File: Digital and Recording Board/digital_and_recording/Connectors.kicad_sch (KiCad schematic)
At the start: 14 parts, among them J1 Headphones, J2 Screen, J3 USB_Breakout, J4 Joystick, J5 Conn_02x20_Odd_Even, U3 Bypass 2, U4 Bypass 1, U5 Output Select

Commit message: updated schematic to use +/-5 DCDC
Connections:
- net +5V: now also C2.2, C4.1, C7.2, U3.4 (V+), U4.4 (V+), U5.4 (V+)
- net Guitar_In: now also J5.25 (Pin_25), J5.26 (Pin_26), J5.27 (Pin_27), J5.28 (Pin_28); no longer J5.37 (Pin_37), J5.38 (Pin_38), J5.39 (Pin_39), J5.40 (Pin_40)
- removed net +6V: C2.2, C4.1, C7.2, J5.13 (Pin_13), J5.14 (Pin_14), J5.15 (Pin_15), J5.16 (Pin_16), U3.4 (V+), U4.4 (V+), U5.4 (V+)
- net -6V renamed -5V
- net -5V: no longer J5.19 (Pin_19), J5.20 (Pin_20), J5.21 (Pin_21), J5.22 (Pin_22)
- no-connect marks 16 -> 24

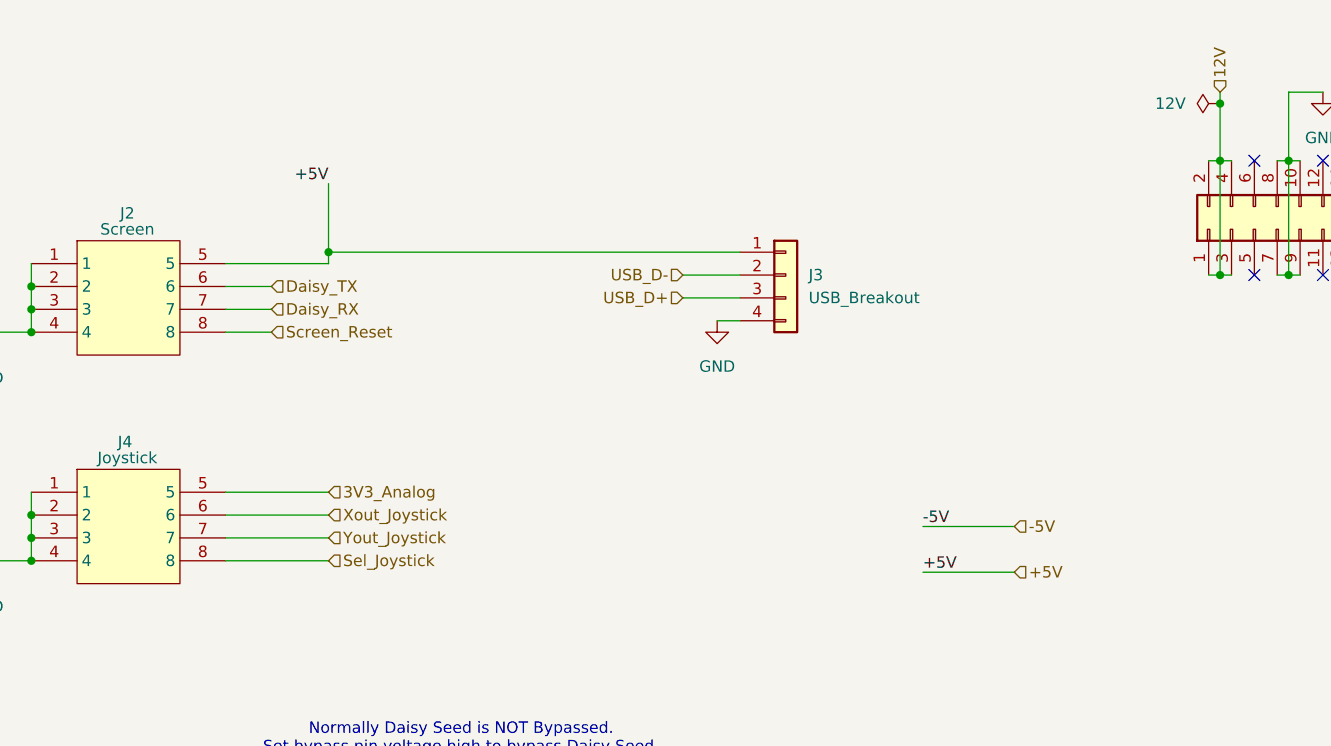
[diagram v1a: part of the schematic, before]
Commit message: modified power for proper amp rating of daisy seed
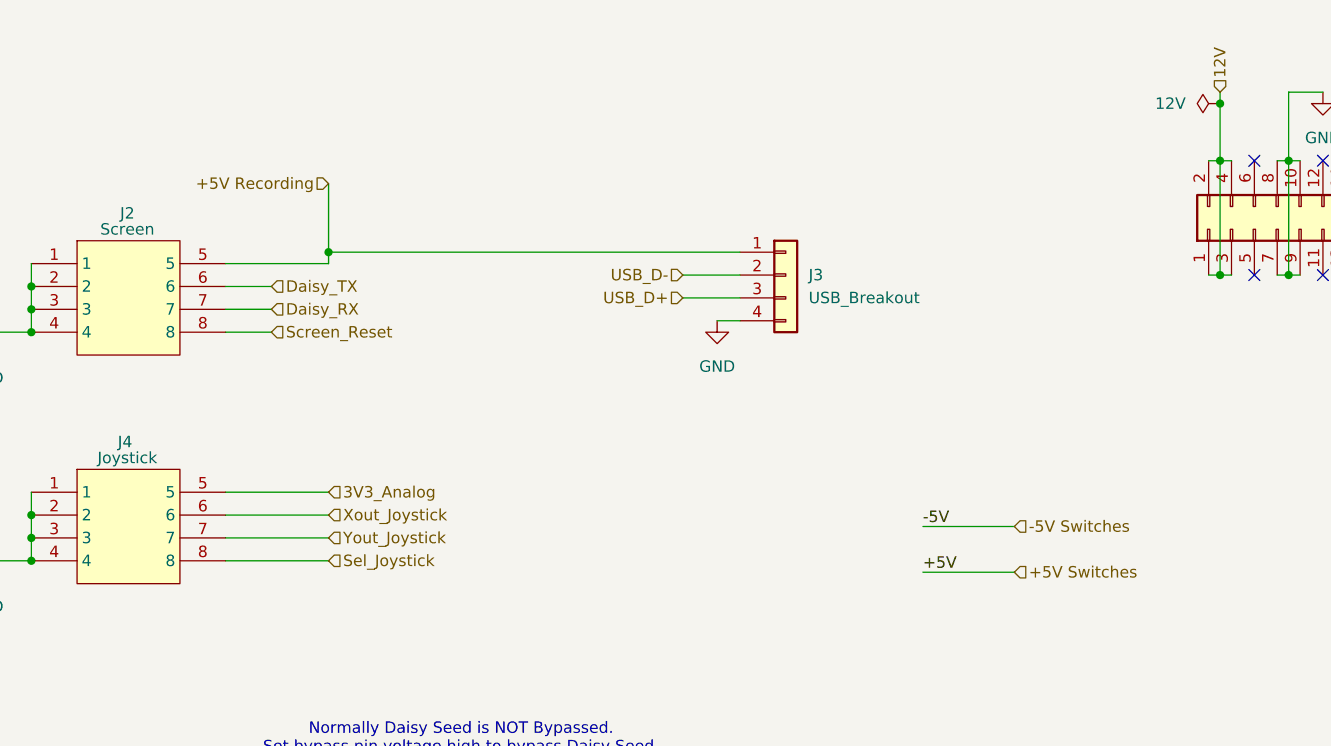
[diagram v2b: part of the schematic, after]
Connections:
- net +5V renamed +5V Switches
- net +5V Switches: no longer J2.5, J3.1 (Pin_1)
- net -5V renamed -5V Switches
- new net +5V Recording: J2.5, J3.1 (Pin_1)
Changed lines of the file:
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@@
-		)
-	)
-	(label "+5V"
-		(at 91.44 41.91 180)
-		(effects
-			(font
-				(size 1.27 1.27)
-			)
-			(justify right bottom)
 		)
 	)
@@
 			)
 			(justify left)
+		)
+	)
+	(hierarchical_label "+5V Recording"
+		(shape input)
+		(at 91.44 41.91 180)
+		(effects
+			(font
+				(size 1.27 1.27)
+			)
+			(justify right)
 		)
 	)
@@
 		)
 	)
-	(hierarchical_label "-5V"
+	(hierarchical_label "-5V Switches"
 		(shape input)
 		(at 167.64 80.01 0)
@@
 		)
 	)
-	(hierarchical_label "+5V"
+	(hierarchical_label "+5V Switches"
 		(shape input)
 		(at 167.64 85.09 0)

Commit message: layout for digital board is essentially complete
current draw for the screen may fuck us if it is too high
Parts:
- C2, C3, C4, C5, C6, C7: footprint Capacitor_SMD:C_0201_0603Metric -> Capacitor_SMD:C_0603_1608Metric
- U3, U4, U5: footprint TS12A12511DCNR:SOT65P280X145-8N -> Kyle's Footprints:SOT65P280X145-8N
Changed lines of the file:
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@@
 			)
 		)
-		(property "Footprint" "TS12A12511DCNR:SOT65P280X145-8N"
+		(property "Footprint" "Kyle's Footprints:SOT65P280X145-8N"
 			(at 232.41 133.35 0)
 			(effects
@@
 			)
 		)
-		(property "Footprint" "TS12A12511DCNR:SOT65P280X145-8N"
+		(property "Footprint" "Kyle's Footprints:SOT65P280X145-8N"
 			(at 163.83 130.81 0)
 			(effects
@@
 			)
 		)
-		(property "Footprint" "Capacitor_SMD:C_0201_0603Metric"
+		(property "Footprint" "Capacitor_SMD:C_0603_1608Metric"
 			(at 96.2152 123.19 0)
 			(effects
@@
 			)
 		)
-		(property "Footprint" "Capacitor_SMD:C_0201_0603Metric"
+		(property "Footprint" "Capacitor_SMD:C_0603_1608Metric"
 			(at 140.6652 123.19 0)
 			(effects
@@
 			)
 		)
-		(property "Footprint" "Capacitor_SMD:C_0201_0603Metric"
+		(property "Footprint" "Capacitor_SMD:C_0603_1608Metric"
 			(at 101.2952 148.59 0)
 			(effects
@@
 			)
 		)
-		(property "Footprint" "Capacitor_SMD:C_0201_0603Metric"
+		(property "Footprint" "Capacitor_SMD:C_0603_1608Metric"
 			(at 140.6652 148.59 0)
 			(effects
@@
 			)
 		)
-		(property "Footprint" "Capacitor_SMD:C_0201_0603Metric"
+		(property "Footprint" "Capacitor_SMD:C_0603_1608Metric"
 			(at 260.0452 148.59 0)
 			(effects
@@
 			)
 		)
-		(property "Footprint" "TS12A12511DCNR:SOT65P280X145-8N"
+		(property "Footprint" "Kyle's Footprints:SOT65P280X145-8N"
 			(at 74.93 133.35 0)
 			(effects
@@
 			)
 		)
-		(property "Footprint" "Capacitor_SMD:C_0201_0603Metric"
+		(property "Footprint" "Capacitor_SMD:C_0603_1608Metric"
 			(at 260.0452 123.19 0)
 			(effects

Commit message: im pushing in case kicad crashes again
also the board was significantly updated
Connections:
- net +5V Recording renamed 5V_Dig
- net 5V_Dig: no longer J3.1 (Pin_1)
- new net 5V_Rec: J3.1 (Pin_1)
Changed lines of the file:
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@@
-	)
-	(junction
-		(at 91.44 49.53)
-		(diameter 0)
-		(color 0 0 0 0)
 	)
 	(junction
@@
 	(wire
 		(pts
+			(xy 137.16 49.53) (xy 132.08 49.53)
+		)
+		(stroke
+			(width 0)
+			(type default)
+		)
+	)
+	(wire
+		(pts
 			(xy 139.7 114.3) (xy 139.7 115.57)
 		)
@@
 	(wire
 		(pts
-			(xy 91.44 49.53) (xy 91.44 50.8)
-		)
-		(stroke
-			(width 0)
-			(type default)
-		)
-	)
-	(wire
-		(pts
 			(xy 219.71 52.07) (xy 220.98 52.07)
 		)
@@
 	(wire
 		(pts
-			(xy 91.44 49.53) (xy 137.16 49.53)
-		)
-		(stroke
-			(width 0)
-			(type default)
-		)
-	)
-	(wire
-		(pts
 			(xy 80.01 55.88) (xy 85.09 55.88)
 		)
@@
 	(wire
 		(pts
-			(xy 91.44 41.91) (xy 91.44 49.53)
+			(xy 91.44 41.91) (xy 91.44 50.8)
 		)
 		(stroke
@@
 		(pts
 			(xy 215.9 82.55) (xy 219.71 82.55)
+		)
+		(stroke
+			(width 0)
+			(type default)
+		)
+	)
+	(wire
+		(pts
+			(xy 132.08 49.53) (xy 132.08 45.72)
 		)
 		(stroke
@@
 		)
 	)
-	(hierarchical_label "+5V Recording"
-		(shape input)
-		(at 91.44 41.91 180)
-		(effects
-			(font
-				(size 1.27 1.27)
-			)
-			(justify right)
-		)
-	)
 	(hierarchical_label "Daisy_TX"
 		(shape input)
@@
 			)
 			(justify left)
+		)
+	)
+	(symbol
+		(lib_id "power:VCC")
+		(at 132.08 45.72 0)
+		(unit 1)
+		(exclude_from_sim no)
+		(in_bom yes)
+		(on_board yes)
+		(dnp no)
+		(fields_autoplaced yes)
+		(property "Reference" "#PWR027"
+			(at 132.08 49.53 0)
+			(effects
+				(font
+					(size 1.27 1.27)
+				)
+				(hide yes)
+			)
+		)
+		(property "Value" "5V_Rec"
+			(at 132.08 40.64 0)
+			(effects
+				(font
+					(size 1.27 1.27)
+				)
+			)
+		)
+		(property "Footprint" ""
+			(at 132.08 45.72 0)
+			(effects
+				(font
+					(size 1.27 1.27)
+				)
+				(hide yes)
+			)
+		)
+		(property "Datasheet" ""
+			(at 132.08 45.72 0)
+			(effects
+				(font
+					(size 1.27 1.27)
+				)
+				(hide yes)
+			)
+		)
+		(property "Description" "Power symbol creates a global label with name \"VCC\""
+			(at 132.08 45.72 0)
+			(effects
+				(font
+					(size 1.27 1.27)
+				)
+				(hide yes)
+			)
+		)
+		(pin "1"
+		)
+		(instances
+			(project ""
+				(path "/5074a352-7a9b-47ff-bda0-b973f990e136/9870da14-8df9-4fc5-b968-74c758b24db3"
+					(reference "#PWR027")
+					(unit 1)
+				)
+			)
 		)
 	)
@@
 					(unit 1)
 				)
+			)
+		)
+	)
+	(symbol
+		(lib_id "power:VCC")
+		(at 91.44 41.91 0)
+		(unit 1)
+		(exclude_from_sim no)
+		(in_bom yes)
+		(on_board yes)
+		(dnp no)
+		(fields_autoplaced yes)
+		(property "Reference" "#PWR026"
+			(at 91.44 45.72 0)
+			(effects
+				(font
+					(size 1.27 1.27)
+				)
+				(hide yes)
+			)
+		)
+		(property "Value" "5V_Dig"
+			(at 91.44 36.83 0)
+			(effects
+				(font
+					(size 1.27 1.27)
+				)
+			)
+		)
+		(property "Footprint" ""
+			(at 91.44 41.91 0)
+			(effects
+				(font
+					(size 1.27 1.27)
+				)
+				(hide yes)
+			)
+		)
+		(property "Datasheet" ""
+			(at 91.44 41.91 0)
+			(effects
+				(font
+					(size 1.27 1.27)
+				)
+				(hide yes)
+			)
+		)
+		(property "Description" "Power symbol creates a global label with name \"VCC\""
+			(at 91.44 41.91 0)
+			(effects
+				(font
+					(size 1.27 1.27)
+				)
+				(hide yes)
+			)
+		)
+		(pin "1"
+		)
+		(instances
+			(project ""
+				(path "/5074a352-7a9b-47ff-bda0-b973f990e136/9870da14-8df9-4fc5-b968-74c758b24db3"
+					(reference "#PWR026")
+					(unit 1)
+				)

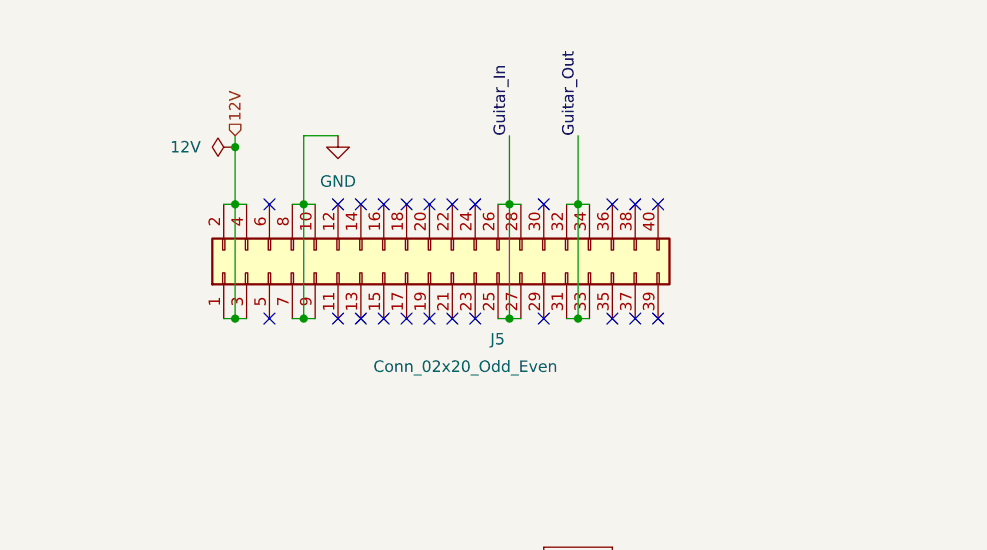
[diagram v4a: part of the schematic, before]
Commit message: updated schematic of digital and recording board to use 2 pin molex for power and guitar signals
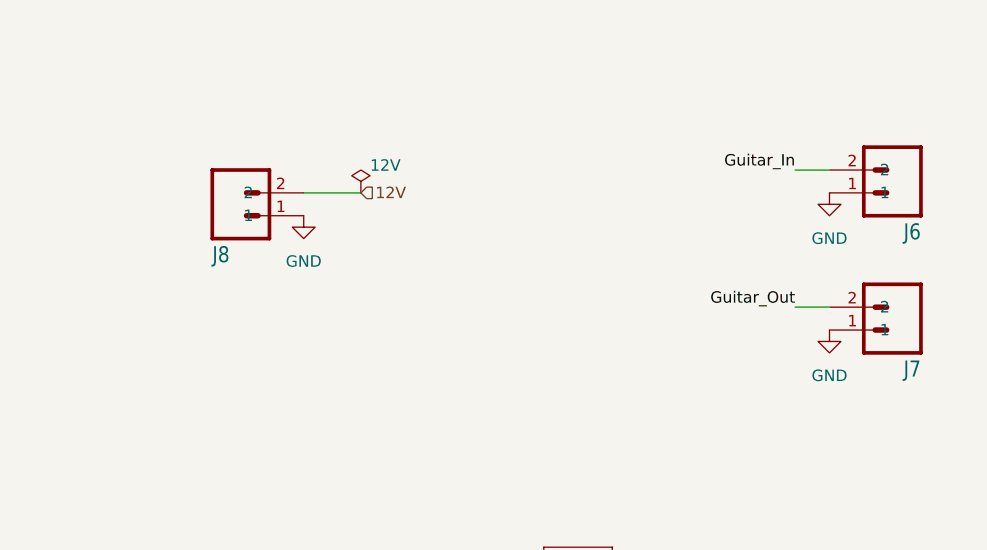
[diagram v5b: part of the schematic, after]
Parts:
- removed J5: Conn_02x20_Odd_Even, Connector_PinHeader_1.00mm:PinHeader_2x20_P1.00mm_Vertical, symbol Connector_Generic:Conn_02x20_Odd_Even
- added J6, J7: MINIFIT-2-VERT, Connector_Molex:Molex_Mini-Fit_Jr_5566-02A_2x01_P4.20mm_Vertical, symbol BMS-Master-Revision8-eagle-import:MINIFIT-2-VERT
- added J8: MINIFIT-2-VERT, Connector_Molex:Molex_Mega-Fit_76829-0102_2x01_P5.70mm_Vertical, symbol BMS-Master-Revision8-eagle-import:MINIFIT-2-VERT
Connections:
- net 12V: now also J8.2
- net GND: now also J6.1, J7.1, J8.1
- net Guitar_In: now also J6.2
- net Guitar_Out: now also J7.2
- no-connect marks 24 -> 0

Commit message: corrected connectors
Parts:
- added H1, H2, H3, H4: MountingHole, MountingHole:MountingHole_2.7mm_M2.5, symbol Mechanical:MountingHole

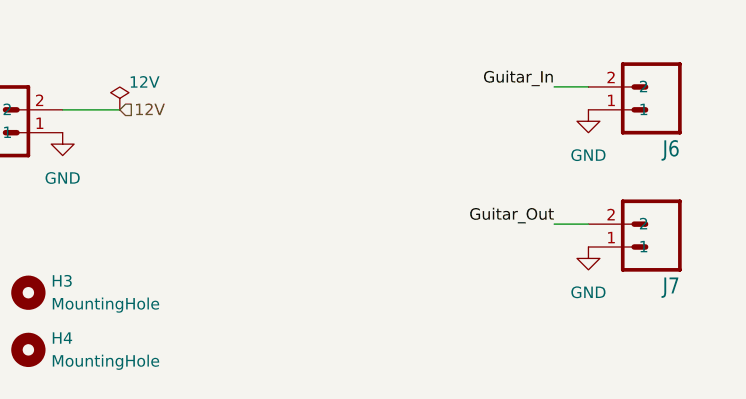
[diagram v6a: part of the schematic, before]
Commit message: added buffers and caps for op-amps on effect boards
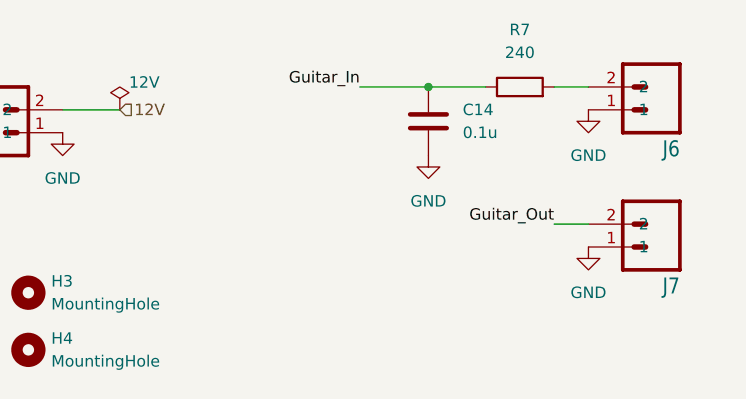
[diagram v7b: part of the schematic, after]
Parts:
- added C14: 0.1u, Capacitor_SMD:C_0603_1608Metric, symbol Device:C
- added R7: 240, Resistor_SMD:R_0603_1608Metric, symbol Device:R
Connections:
- net GND: now also C14.2
- net Guitar_In: now also C14.1, R7.1; no longer J6.2
- new net: J6.2, R7.2
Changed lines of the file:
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@@
+	)
+	(junction
+		(at 238.76 35.56)
+		(diameter 0)
+		(color 0 0 0 0)
 	)
 	(junction
@@
 	(wire
 		(pts
+			(xy 238.76 35.56) (xy 245.11 35.56)
+		)
+		(stroke
+			(width 0)
+			(type default)
+		)
+	)
+	(wire
+		(pts
 			(xy 92.71 128.27) (xy 96.52 128.27)
 		)
@@
 		(pts
 			(xy 212.09 133.35) (xy 214.63 133.35)
+		)
+		(stroke
+			(width 0)
+			(type default)
+		)
+	)
+	(wire
+		(pts
+			(xy 231.14 35.56) (xy 238.76 35.56)
 		)
 		(stroke
@@
 	)
 	(label "Guitar_In"
-		(at 252.73 35.56 180)
+		(at 231.14 35.56 180)
 		(effects
 			(font
@@
 	)
 	(symbol
+		(lib_id "Device:C")
+		(at 238.76 39.37 0)
+		(unit 1)
+		(exclude_from_sim no)
+		(in_bom yes)
+		(on_board yes)
+		(dnp no)
+		(fields_autoplaced yes)
+		(property "Reference" "C14"
+			(at 242.57 38.0999 0)
+			(effects
+				(font
+					(size 1.27 1.27)
+				)
+				(justify left)
+			)
+		)
+		(property "Value" "0.1u"
+			(at 242.57 40.6399 0)
+			(effects
+				(font
+					(size 1.27 1.27)
+				)
+				(justify left)
+			)
+		)
+		(property "Footprint" "Capacitor_SMD:C_0603_1608Metric"
+			(at 239.7252 43.18 0)
+			(effects
+				(font
+					(size 1.27 1.27)
+				)
+				(hide yes)
+			)
+		)
+		(property "Datasheet" "~"
+			(at 238.76 39.37 0)
+			(effects
+				(font
+					(size 1.27 1.27)
+				)
+				(hide yes)
+			)
+		)
+		(property "Description" "Unpolarized capacitor"
+			(at 238.76 39.37 0)
+			(effects
+				(font
+					(size 1.27 1.27)
+				)
+				(hide yes)
+			)
+		)
+		(pin "2"
+		)
+		(pin "1"
+		)
+		(instances
+			(project ""
+				(path "/5074a352-7a9b-47ff-bda0-b973f990e136/9870da14-8df9-4fc5-b968-74c758b24db3"
+					(reference "C14")
+					(unit 1)
+				)
+			)
+		)
+	)
+	(symbol
 		(lib_id "BMS-Master-Revision8-eagle-import:MINIFIT-2-VERT")
 		(at 187.96 43.18 0)
@@
 	)
 	(symbol
+		(lib_id "power:GND")
+		(at 238.76 43.18 0)
+		(unit 1)
+		(exclude_from_sim no)
+		(in_bom yes)
+		(on_board yes)
+		(dnp no)
+		(fields_autoplaced yes)
+		(property "Reference" "#PWR030"
+			(at 238.76 49.53 0)
+			(effects
+				(font
+					(size 1.27 1.27)
+				)
+				(hide yes)
+			)
+		)
+		(property "Value" "GND"
+			(at 238.76 48.26 0)
+			(effects
+				(font
+					(size 1.27 1.27)
+				)
+			)
+		)
+		(property "Footprint" ""
+			(at 238.76 43.18 0)
+			(effects
+				(font
+					(size 1.27 1.27)
+				)
+				(hide yes)
+			)
+		)
+		(property "Datasheet" ""
+			(at 238.76 43.18 0)
+			(effects
+				(font
+					(size 1.27 1.27)
+				)
+				(hide yes)
+			)
+		)
+		(property "Description" "Power symbol creates a global label with name \"GND\" , ground"
+			(at 238.76 43.18 0)
+			(effects
+				(font
+					(size 1.27 1.27)
+				)
+				(hide yes)
+			)
+		)
+		(pin "1"
+		)
+		(instances
+			(project "digital_and_recording"
+				(path "/5074a352-7a9b-47ff-bda0-b973f990e136/9870da14-8df9-4fc5-b968-74c758b24db3"
+					(reference "#PWR030")
+					(unit 1)
+				)
+			)
+		)
+	)
+	(symbol
 		(lib_id "BMS-Master-Revision8-eagle-import:MINIFIT-2-VERT")
 		(at 266.7 55.88 180)
@@
 					(unit 1)
 				)
+			)
+		)
+	)
+	(symbol
+		(lib_id "Device:R")
+		(at 248.92 35.56 90)
+		(unit 1)
+		(exclude_from_sim no)
+		(in_bom yes)
+		(on_board yes)
+		(dnp no)
+		(fields_autoplaced yes)
+		(property "Reference" "R7"
+			(at 248.92 29.21 90)
+			(effects
+				(font
+					(size 1.27 1.27)
+				)
+			)
+		)
+		(property "Value" "240"
+			(at 248.92 31.75 90)
+			(effects
+				(font
+					(size 1.27 1.27)
+				)
+			)
+		)
+		(property "Footprint" "Resistor_SMD:R_0603_1608Metric"
+			(at 248.92 37.338 90)
+			(effects
+				(font
+					(size 1.27 1.27)
+				)
+				(hide yes)
+			)
+		)
+		(property "Datasheet" "~"
+			(at 248.92 35.56 0)
+			(effects
+				(font
+					(size 1.27 1.27)
+				)
+				(hide yes)
+			)
+		)
+		(property "Description" "Resistor"
+			(at 248.92 35.56 0)
+			(effects
+				(font
+					(size 1.27 1.27)
+				)
+				(hide yes)
+			)
+		)
+		(pin "1"
+		)
+		(pin "2"
+		)
+		(instances
+			(project ""
+				(path "/5074a352-7a9b-47ff-bda0-b973f990e136/9870da14-8df9-4fc5-b968-74c758b24db3"
+					(reference "R7")
+					(unit 1)
+				)

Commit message: fixed it
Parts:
- J3: footprint Connector_PinHeader_1.00mm:PinHeader_1x04_P1.00mm_Vertical -> Connector_PinHeader_2.54mm:PinHeader_1x04_P2.54mm_Vertical
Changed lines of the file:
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@@
 			)
 		)
-		(property "Footprint" "Connector_PinHeader_1.00mm:PinHeader_1x04_P1.00mm_Vertical"
+		(property "Footprint" "Connector_PinHeader_2.54mm:PinHeader_1x04_P2.54mm_Vertical"
 			(at 142.24 52.07 0)
 			(effects
